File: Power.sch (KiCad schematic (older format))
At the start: 68 parts, among them J3 ESTOP, J4 PWR, J5 Conn_ARM_JTAG_SWD_10, J7 FAN, Q1 MMBT5401LT1G, Q2 PSMN4R8-100BSEJ, Q3 MMBT3904, Q5 PSMN4R8-100BSEJ, Q7 NTS4001NT1G, U10 LMZ21700SIL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

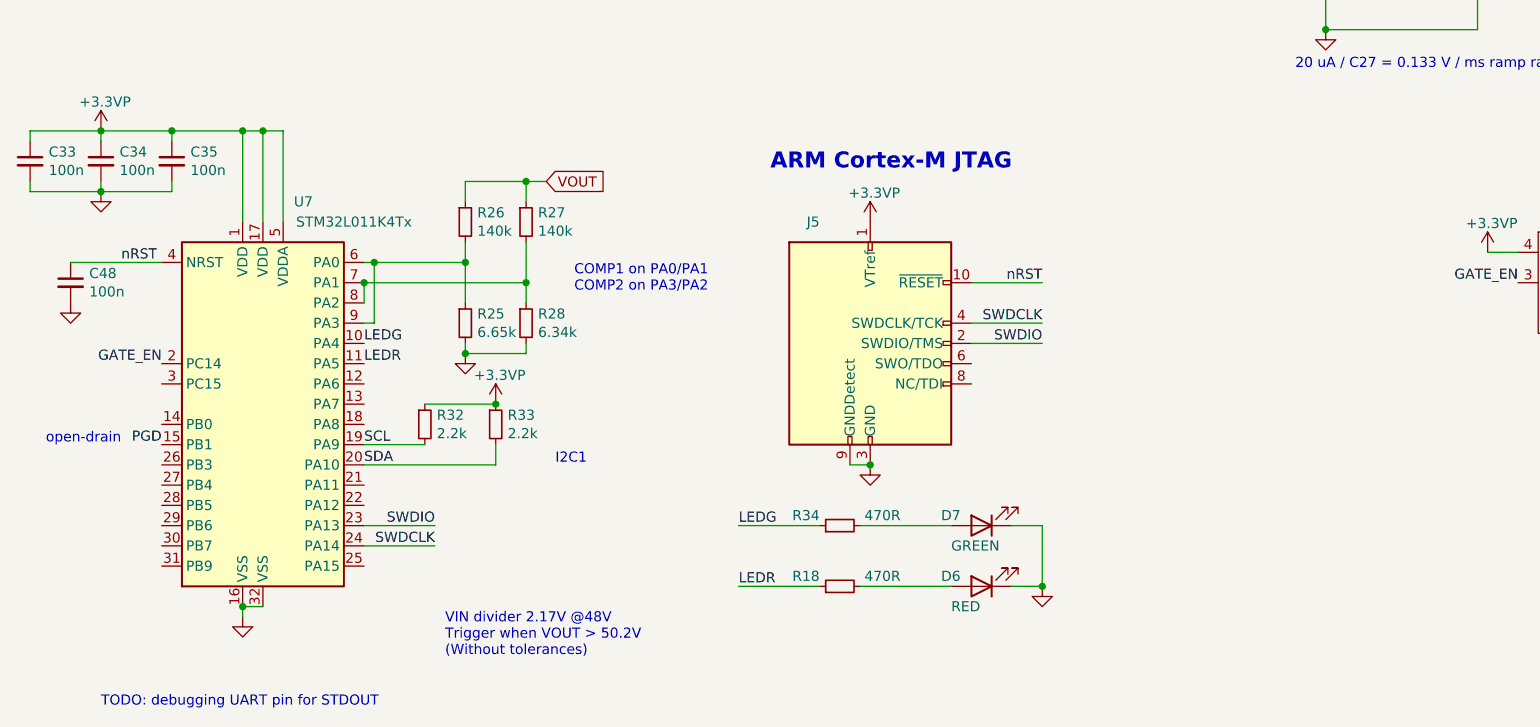
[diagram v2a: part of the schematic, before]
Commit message: layout tweaks. add debugging headers.
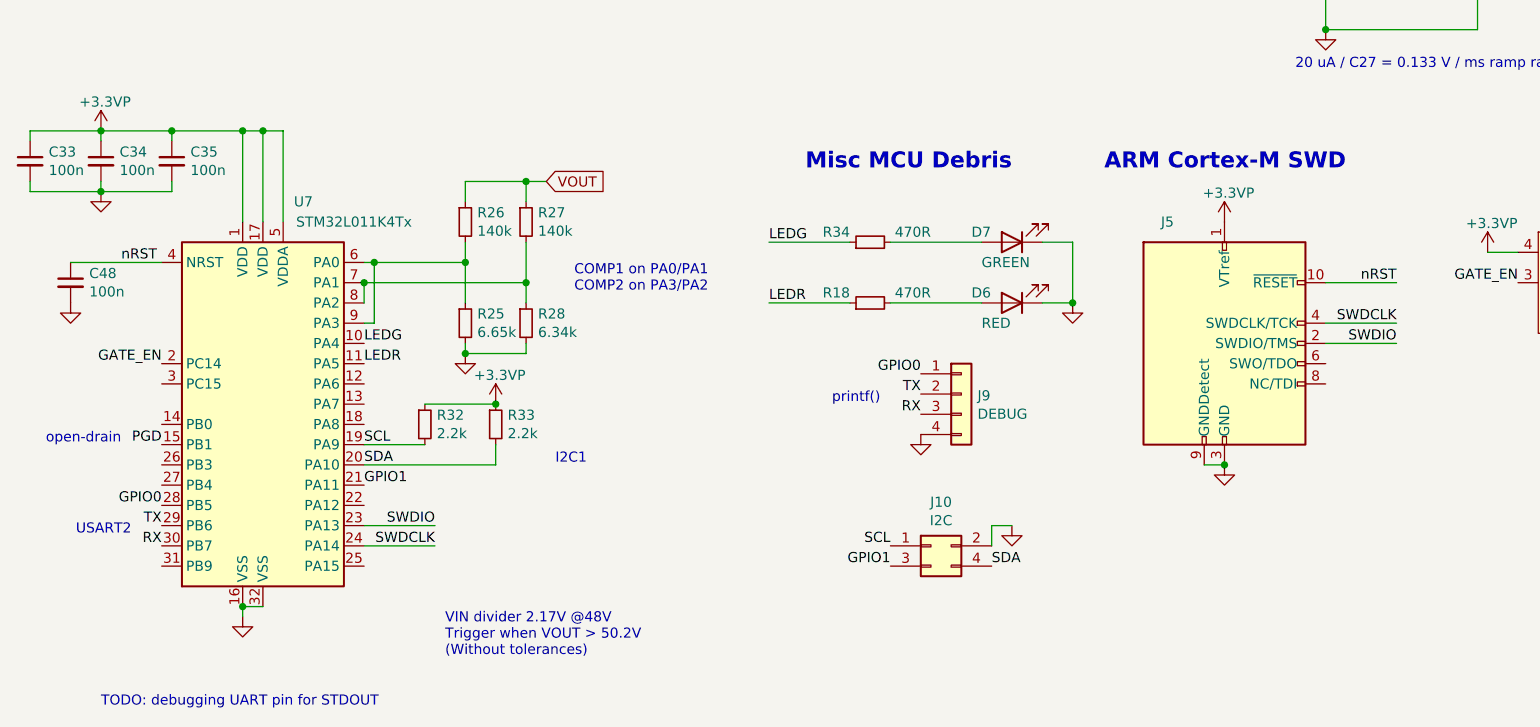
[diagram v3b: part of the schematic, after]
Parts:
- added J10: I2C, Connector_PinHeader_2.54mm:PinHeader_2x02_P2.54mm_Vertical, symbol Connector_Generic:Conn_02x02_Odd_Even
- added J9: DEBUG, Connector_PinHeader_2.54mm:PinHeader_1x04_P2.54mm_Vertical, symbol Connector_Generic:Conn_01x04
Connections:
- net GND: now also J10.2 (Pin_2), J9.4 (Pin_4)
- net SCL: now also J10.1 (Pin_1)
- net SDA: now also J10.4 (Pin_4)
- net GPIO1: now reaches U7.21 (PA11)
- net GPIO1: now also J10.3 (Pin_3)
- net GPIO0: now reaches U7.28 (PB5)
- net GPIO0: now also J9.1 (Pin_1)
- net TX: now reaches U7.29 (PB6)
- net TX: now also J9.2 (Pin_2)
- net RX: now reaches U7.30 (PB7)
- net RX: now also J9.3 (Pin_3)
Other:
- note added: "ARM Cortex-M SWD"
- note added: "Misc MCU Debris"
- note added: "USART2"
- note added: "printf()"
- note removed: "ARM Cortex-M JTAG"
- moved on the sheet: D6, D7, J5, R18, R34
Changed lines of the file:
@@
 Connection ~ 4250 1100
 Connection ~ 4700 1100
-Connection ~ 4800 6400
 Connection ~ 4850 3600
 Connection ~ 5150 1100
@@
 Connection ~ 5450 1450
 Connection ~ 5550 2900
-Connection ~ 5650 7000
+Connection ~ 5800 5600
 Connection ~ 6100 1100
 Connection ~ 6100 1450
 Connection ~ 6550 1100
+Connection ~ 6550 6400
 Connection ~ 6650 3300
 Connection ~ 6925 1100
@@
 	4150 3650 4150 3600
 Wire Wire Line
-	4150 6700 4550 6700
-Wire Wire Line
-	4150 7000 4550 7000
-Wire Wire Line
 	4250 1100 4250 1900
 Wire Wire Line
 	4250 1100 4700 1100
 Wire Wire Line
+	4300 5300 4700 5300
+Wire Wire Line
+	4300 5600 4700 5600
+Wire Wire Line
 	4350 1550 4350 1900
 Wire Wire Line
@@
 	4700 1100 5150 1100
 Wire Wire Line
-	4700 6400 4800 6400
-Wire Wire Line
 	4750 2300 5900 2300
 Wire Wire Line
@@
 	5200 3600 5550 3600
 Wire Wire Line
-	5200 6700 4750 6700
-Wire Wire Line
-	5200 7000 4750 7000
-Wire Wire Line
 	5250 3300 5200 3300
 Wire Wire Line
-	5300 5500 5650 5500
+	5350 5300 4900 5300
+Wire Wire Line
+	5350 5600 4900 5600
+Wire Wire Line
+	5400 6700 5400 6800
 Wire Wire Line
 	5450 1100 6100 1100
@@
 	5450 1400 5450 1450
 Wire Wire Line
-	5500 6700 5650 6700
+	5500 6700 5400 6700
 Wire Wire Line
 	5550 2400 5550 2650
@@
 	5550 3500 5550 3600
 Wire Wire Line
-	5650 5700 5300 5700
-Wire Wire Line
-	5650 5800 5300 5800
-Wire Wire Line
-	5650 6700 5650 7000
-Wire Wire Line
-	5650 7000 5500 7000
+	5650 5300 5800 5300
+Wire Wire Line
+	5800 5300 5800 5600
+Wire Wire Line
+	5800 5600 5650 5600
 Wire Wire Line
 	5900 2650 5900 2300
@@
 	6100 1450 6550 1450
 Wire Wire Line
+	6450 6400 6550 6400
+Wire Wire Line
 	6550 1100 6550 1150
 Wire Wire Line
@@
 	7050 4250 7800 4250
 Wire Wire Line
+	7050 5500 7400 5500
+Wire Wire Line
 	7300 1400 7300 1100
 Wire Wire Line
@@
 Wire Wire Line
 	7300 2700 7500 2700
+Wire Wire Line
+	7400 5700 7050 5700
+Wire Wire Line
+	7400 5800 7050 5800
 Wire Wire Line
 	7500 1100 7500 1400
@@
 Text Notes 1100 6300 2    50   ~ 0
 open-drain
+Text Notes 1150 6750 2    50   ~ 0
+USART2
 Text Notes 1650 3000 0    50   ~ 0
 TODO: gate TVS?
@@
 Text Notes 4000 5550 2    50   ~ 0
 COMP1 on PA0/PA1\nCOMP2 on PA3/PA2
+Text Notes 4850 6100 2    50   ~ 0
+printf()
 Text Notes 4970 3840 0    50   ~ 0
 18.9 V threshold Power Good
@@
 Schottky diode to eat\nkickback energy at power-off
 Text Notes 5500 4950 2    79   ~ 16
-ARM Cortex-M JTAG
+Misc MCU Debris
 Text Notes 5650 3100 2    50   ~ 0
 I2C addr: ZZZ = 0x40
@@
 Text Notes 6850 2200 2    50   ~ 0
 RT floating = 500 kHz
+Text Notes 7150 4950 2    79   ~ 16
+ARM Cortex-M SWD
 Text Notes 8200 4450 2    50   ~ 0
 20 uA / C27 = 0.133 V / ms ramp rate
@@
 Text Label 1300 6300 2    50   ~ 0
 PGD
+Text Label 1300 6600 2    50   ~ 0
+GPIO0
+Text Label 1300 6700 2    50   ~ 0
+TX
+Text Label 1300 6800 2    50   ~ 0
+RX
 Text Label 1700 1100 2    50   ~ 0
 VIN
@@
 Text Label 2300 6400 0    50   ~ 0
 SDA
+Text Label 2300 6500 0    50   ~ 0
+GPIO1
 Text Label 2650 6700 2    50   ~ 0
 SWDIO
@@
 Text Label 3800 1400 0    50   ~ 0
 GATE
-Text Label 4150 6700 0    50   ~ 0
+Text Label 4300 5300 0    50   ~ 0
 LEDG
-Text Label 4150 7000 0    50   ~ 0
+Text Label 4300 5600 0    50   ~ 0
 LEDR
 Text Label 4400 1550 0    50   ~ 0
@@
 Text Label 4800 2100 0    50   ~ 0
 PGD
+Text Label 4900 6800 2    50   ~ 0
+SCL
+Text Label 4900 6900 2    50   ~ 0
+GPIO1
 Text Label 5050 2500 2    50   ~ 0
 LM_VDD
-Text Label 5650 5500 2    50   ~ 0
-nRST
-Text Label 5650 5700 2    50   ~ 0
-SWDCLK
-Text Label 5650 5800 2    50   ~ 0
-SWDIO
+Text Label 5050 5950 2    50   ~ 0
+GPIO0
+Text Label 5050 6050 2    50   ~ 0
+TX
+Text Label 5050 6150 2    50   ~ 0
+RX
+Text Label 5400 6900 0    50   ~ 0
+SDA
 Text Label 6450 3300 0    50   ~ 0
 GATE
+Text Label 7400 5500 2    50   ~ 0
+nRST
+Text Label 7400 5700 2    50   ~ 0
+SWDCLK
+Text Label 7400 5800 2    50   ~ 0
+SWDIO
 Text Label 8000 5500 2    50   ~ 0
 GATE_EN
@@
 L power:+3.3VP #PWR0153
 U 1 1 5D5EB6F2
-P 4800 5200
-F 0 "#PWR0153" H 4950 5150 50  0001 C CNN
-F 1 "+3.3VP" H 4820 5343 50  0000 C CNN
-F 2 "" H 4800 5200 50  0001 C CNN
-F 3 "" H 4800 5200 50  0001 C CNN
-	1    4800 5200
+P 6550 5200
+F 0 "#PWR0153" H 6700 5150 50  0001 C CNN
+F 1 "+3.3VP" H 6570 5343 50  0000 C CNN
+F 2 "" H 6550 5200 50  0001 C CNN
+F 3 "" H 6550 5200 50  0001 C CNN
+	1    6550 5200
 	1    0    0    -1
 $EndComp
@@
 $EndComp
 $Comp
-L power:GND #PWR0139
-U 1 1 5E51739C
-P 4800 6400
-F 0 "#PWR0139" H 4800 6150 50  0001 C CNN
-F 1 "GND" H 4805 6227 50  0001 C CNN
-F 2 "" H 4800 6400 50  0001 C CNN
-F 3 "" H 4800 6400 50  0001 C CNN
-	1    4800 6400
+L power:GND #PWR0152
+U 1 1 5E55447C
+P 5050 6250
+F 0 "#PWR0152" H 5050 6000 50  0001 C CNN
+F 1 "GND" H 5055 6077 50  0001 C CNN
+F 2 "" H 5050 6250 50  0001 C CNN
+F 3 "" H 5050 6250 50  0001 C CNN
+	1    5050 6250
 	-1   0    0    -1
 $EndComp
@@
 $EndComp
 $Comp
+L power:GND #PWR0155
+U 1 1 5E562944
+P 5500 6700
+F 0 "#PWR0155" H 5500 6450 50  0001 C CNN
+F 1 "GND" H 5505 6527 50  0001 C CNN
+F 2 "" H 5500 6700 50  0001 C CNN
+F 3 "" H 5500 6700 50  0001 C CNN
+	1    5500 6700
+	-1   0    0    -1
+$EndComp
+$Comp
 L power:GND #PWR0149
 U 1 1 5E590701
-P 5650 7000
-F 0 "#PWR0149" H 5650 6750 50  0001 C CNN
-F 1 "GND" H 5655 6827 50  0001 C CNN
-F 2 "" H 5650 7000 50  0001 C CNN
-F 3 "" H 5650 7000 50  0001 C CNN
-	1    5650 7000
+P 5800 5600
+F 0 "#PWR0149" H 5800 5350 50  0001 C CNN
+F 1 "GND" H 5805 5427 50  0001 C CNN
+F 2 "" H 5800 5600 50  0001 C CNN
+F 3 "" H 5800 5600 50  0001 C CNN
+	1    5800 5600
+	-1   0    0    -1
+$EndComp
+$Comp
+L power:GND #PWR0139
+U 1 1 5E51739C
+P 6550 6400
+F 0 "#PWR0139" H 6550 6150 50  0001 C CNN
+F 1 "GND" H 6555 6227 50  0001 C CNN
+F 2 "" H 6550 6400 50  0001 C CNN
+F 3 "" H 6550 6400 50  0001 C CNN
+	1    6550 6400
 	-1   0    0    -1
 $EndComp
@@
 L Device:R_Small R34
 U 1 1 5DD84AA4
-P 4650 6700
-F 0 "R34" V 4700 6800 50  0000 L CNN
-F 1 "470R" V 4700 6400 50  0000 L CNN
-F 2 "Resistor_SMD:R_0603_1608Metric" H 4650 6700 50  0001 C CNN
-F 3 "~" H 4650 6700 50  0001 C CNN
-	1    4650 6700
+P 4800 5300
+F 0 "R34" V 4850 5400 50  0000 L CNN
+F 1 "470R" V 4850 5000 50  0000 L CNN
+F 2 "Resistor_SMD:R_0603_1608Metric" H 4800 5300 50  0001 C CNN
+F 3 "~" H 4800 5300 50  0001 C CNN
+	1    4800 5300
 	0    -1   -1   0
 $EndComp
@@
 L Device:R_Small R18
 U 1 1 5E58F9CA
-P 4650 7000
-F 0 "R18" V 4700 7100 50  0000 L CNN
-F 1 "470R" V 4700 6700 50  0000 L CNN
-F 2 "Resistor_SMD:R_0603_1608Metric" H 4650 7000 50  0001 C CNN
-F 3 "~" H 4650 7000 50  0001 C CNN
-	1    4650 7000
+P 4800 5600
+F 0 "R18" V 4850 5700 50  0000 L CNN
+F 1 "470R" V 4850 5300 50  0000 L CNN
+F 2 "Resistor_SMD:R_0603_1608Metric" H 4800 5600 50  0001 C CNN
+F 3 "~" H 4800 5600 50  0001 C CNN
+	1    4800 5600
 	0    -1   -1   0
 $EndComp
@@
 L Device:LED D7
 U 1 1 5DD84AB5
-P 5350 6700
-F 0 "D7" H 5550 6650 50  0000 R CNN
-F 1 "GREEN" H 5500 6800 50  0000 R CNN
-F 2 "LED_SMD:LED_0603_1608Metric" H 5350 6700 50  0001 C CNN
-F 3 "~" H 5350 6700 50  0001 C CNN
-	1    5350 6700
+P 5500 5300
+F 0 "D7" H 5700 5250 50  0000 R CNN
+F 1 "GREEN" H 5650 5400 50  0000 R CNN
+F 2 "LED_SMD:LED_0603_1608Metric" H 5500 5300 50  0001 C CNN
+F 3 "~" H 5500 5300 50  0001 C CNN
+	1    5500 5300
 	-1   0    0    1
 $EndComp
@@
 L Device:LED D6
 U 1 1 5E58F9DF
-P 5350 7000
-F 0 "D6" H 5550 6950 50  0000 R CNN
-F 1 "RED" H 5500 7100 50  0000 R CNN
-F 2 "LED_SMD:LED_0603_1608Metric" H 5350 7000 50  0001 C CNN
-F 3 "~" H 5350 7000 50  0001 C CNN
-	1    5350 7000
+P 5500 5600
+F 0 "D6" H 5700 5550 50  0000 R CNN
+F 1 "RED" H 5650 5700 50  0000 R CNN
+F 2 "LED_SMD:LED_0603_1608Metric" H 5500 5600 50  0001 C CNN
+F 3 "~" H 5500 5600 50  0001 C CNN
+	1    5500 5600
 	-1   0    0    1
 $EndComp
@@
 	1    1350 1200
 	-1   0    0    -1
+$EndComp
+$Comp
+L Connector_Generic:Conn_01x04 J9
+U 1 1 5E553C28
+P 5250 6050
+F 0 "J9" H 5330 6042 50  0000 L CNN
+F 1 "DEBUG" H 5330 5951 50  0000 L CNN
+F 2 "Connector_PinHeader_2.54mm:PinHeader_1x04_P2.54mm_Vertical" H 5250 6050 50  0001 C CNN
+F 3 "~" H 5250 6050 50  0001 C CNN
+	1    5250 6050
+	1    0    0    -1
+$EndComp
+$Comp
+L Connector_Generic:Conn_02x02_Odd_Even J10
+U 1 1 5E569A0C
+P 5100 6800
+F 0 "J10" H 5150 7016 50  0000 C CNN
+F 1 "I2C" H 5150 6925 50  0000 C CNN
+F 2 "Connector_PinHeader_2.54mm:PinHeader_2x02_P2.54mm_Vertical" H 5100 6800 50  0001 C CNN
+F 3 "~" H 5100 6800 50  0001 C CNN
+	1    5100 6800
+	1    0    0    -1
 $EndComp
 $Comp
@@
 L Connector:Conn_ARM_JTAG_SWD_10 J5
 U 1 1 5D5E762E
-P 4800 5800
-F 0 "J5" H 4550 6400 50  0000 R CNN
-F 1 "Conn_ARM_JTAG_SWD_10" H 4357 5755 50  0001 R CNN
-F 2 "Connector_PinHeader_1.27mm:PinHeader_2x05_P1.27mm_Vertical" H 4800 5800 50  0001 C CNN
-F 3 "http://infocenter.arm.com/help/topic/com.arm.doc.ddi0314h/DDI0314H_coresight_components_trm.pdf" V 4450 4550 50  0001 C CNN
-	1    4800 5800
-	1    0    0    -1
-$EndComp
+P 6550 5800
+F 0 "J5" H 6300 6400 50  0000 R CNN
+F 1 "Conn_ARM_JTAG_SWD_10" H 6107 5755 50  0001 R CNN
+F 2 "Connector_PinHeader_1.27mm:PinHeader_2x05_P1.27mm_Vertical" H 6550 5800 50  0001 C CNN
+F 3 "http://infocenter.arm.com/help/topic/com.arm.doc.ddi0314h/DDI0314H_coresight_components_trm.pdf" V 6200 4550 50  0001 C CNN
+	1    6550 5800
+	1    0    0    -1
+$EndComp

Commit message: ready to generate CAM
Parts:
- C27: D1N (none) -> Digikey; D1PN (none) -> 399-17949-1-ND; MFN (none) -> KEMET; MPN (none) -> C1206C154KARACAUTO; Maximum Voltage (none) -> 250 V; Tolerance (none) -> 10%
- C28: D1N (none) -> Digikey; D1PN (none) -> 478-1529-1-ND; MFN (none) -> AVX; MPN (none) -> 12061C104KAT2A; Maximum Voltage (none) -> 100 V; Tolerance (none) -> 10%
- C29, C30: value 1uF -> 1u; D1N (none) -> Digikey; D1PN (none) -> 311-1445-1-ND; MFN (none) -> Yageo; MPN (none) -> CC0603KRX5R8BB105
- C31, C33, C34, C35, C47, C48: D1N (none) -> Digikey; D1PN (none) -> 311-1344-1-ND; MFN (none) -> Yageo; MPN (none) -> CC0603KRX7R9BB104
- C32: Maximum Voltage (none) -> 80 V; Tolerance (none) -> 20%
- C36: value 1nF -> 1n; D1N (none) -> Digikey; D1PN (none) -> 311-1080-1-ND; MFN (none) -> Yageo; MPN (none) -> CC0603KRX7R9BB102
- C37, C39: D1N (none) -> Digikey; D1PN (none) -> 311-1445-1-ND; MFN (none) -> Yageo; MPN (none) -> CC0603KRX5R8BB105
- C38: D1N (none) -> Digikey; D1PN (none) -> 311-1451-1-ND; MFN (none) -> Yageo; MPN (none) -> CC0603KRX5R6BB225; Maximum Voltage (none) -> 10 V; Tolerance (none) -> 10%
- C40: footprint Capacitor_SMD:C_1210_3225Metric -> Capacitor_SMD:C_1206_3216Metric; D1N (none) -> Digikey; D1PN (none) -> 490-18620-1-ND; MFN (none) -> Murata; MPN (none) -> GRM31CC72A475KE11L; Maximum Voltage (none) -> 100 V; Tolerance (none) -> 10%
- C41: D1N (none) -> Digikey; D1PN (none) -> 311-3365-1-ND; MFN (none) -> Yageo; MPN (none) -> CC0603KRX5R8BB474; Maximum Voltage (none) -> 25 V; Tolerance (none) -> 10%
- C42: footprint Capacitor_SMD:C_1210_3225Metric -> Capacitor_SMD:C_1206_3216Metric; Capacitance 22u -> (none); D1PN 1276-1101-1-ND -> 1276-3047-1-ND; MPN CL32A226KAJNNNE -> CL31A226KAHNNNE; Maximum Voltage 25V -> 25 V
- C43: Capacitance 22u -> (none); D1PN 1276-1101-1-ND -> 1276-3047-1-ND; MPN CL32A226KAJNNNE -> CL31A226KAHNNNE; Maximum Voltage 25V -> 25 V
- C44: Capacitance 4n7 -> (none); D1PN (none) -> 311-3366-1-ND; MFN (none) -> Yageo; MPN (none) -> CC0603KRX7R0BB472; Maximum Voltage 25V -> 25 V
- C45: Capacitance 22u -> (none); D1PN 1276-1101-1-ND -> 490-5528-1-ND; MFN Samsung -> Murata; MPN CL32A226KAJNNNE -> GRM31CR61A476ME15L; Maximum Voltage 6.3V -> 10 V
- C46: D1N (none) -> Digikey; D1PN (none) -> 1276-2344-1-ND; MFN (none) -> Samsung; MPN (none) -> CL10C820JC81PNC; Maximum Voltage (none) -> 100 V; Tolerance (none) -> 5%
- D6: D1N (none) -> Digikey; D1PN (none) -> 732-4978-1-ND; MFN (none) -> Wurth; MPN (none) -> 150060RS75000
- D7: D1N (none) -> Digikey; D1PN (none) -> 732-4980-1-ND; MFN (none) -> Wurth; MPN (none) -> 150060VS75000
- J10, J9: D1N (none) -> DNP; D1PN (none) -> DNP; MFN (none) -> DNP; MPN (none) -> DNP
- J3: D1N (none) -> Digikey; D1PN (none) -> WM15141-ND; MFN (none) -> Molex; MPN (none) -> 1053131302
- J4: D1N (none) -> Digikey; D1PN (none) -> WM14310CT-ND; MFN (none) -> Molex; MPN (none) -> 436500214
- J5: D1N (none) -> Digikey; D1PN (none) -> S9015E-05-ND; MFN (none) -> Sullins; MPN (none) -> GRPB052VWVN-RC
- J7: D1N digikey -> Digikey; MPN 0022232031 -> 22232031
- L1: D1N (none) -> Digikey; D1PN (none) -> 732-1199; MFN (none) -> Wurth; MPN (none) -> 744777920
- Q5: D1N (none) -> Digikey; D1PN (none) -> 1727-1103-1-ND; MFN (none) -> NXP; MPN (none) -> PSMN4R8-100BSEJ
- R10, R12, R15, R26, R27: D1N (none) -> Digikey; D1PN (none) -> P140KDBCT-ND; MFN (none) -> Panasonic; MPN (none) -> ERA-3AEB1403V; Tolerance (none) -> 0.1%
- R11: value 6k5 -> 6k49; D1N (none) -> Digikey; D1PN (none) -> P6.49KDBCT-ND; MFN (none) -> Panasonic; MPN (none) -> ERA-3AEB6491V; Tolerance (none) -> 0.1%
- R13: D1N (none) -> Digikey; D1PN (none) -> P25.5KDBCT-ND; MFN (none) -> Panasonic; MPN (none) -> ERA-3AEB2552V; Tolerance (none) -> 0.1%
- R16, R17: D1N (none) -> Digikey; D1PN (none) -> P21KDBCT-ND; MFN (none) -> Panasonic; MPN (none) -> ERA-3AEB2102V; Tolerance (none) -> 0.1%
- R18, R34: D1N (none) -> Digikey; D1PN (none) -> 311-470HRCT-ND; MFN (none) -> Yageo; MPN (none) -> RC0603FR-07470RL; Tolerance (none) -> 1%
- R19: D1N (none) -> Digikey; D1PN (none) -> 311-33.0HRCT-ND; MFN (none) -> Yageo; MPN (none) -> RC0603FR-0733RL; Tolerance (none) -> 1%
- R21: D1N (none) -> Digikey; D1PN (none) -> 696-1107-5-ND; MFN (none) -> Riedon; MPN (none) -> PF2472-10RF1
- R24: D1PN 311-453KHRCT-ND -> 311-1.00MHRCT-ND; MPN RC0603FR-07453KL -> RC0603FR-071ML; Maximum Power 0.1W -> (none); Resistance 1100000.0ohm -> (none)
- R25: D1N (none) -> Digikey; D1PN (none) -> P6.65KDBCT-ND; MFN (none) -> Panasonic; MPN (none) -> ERA-3AEB6651V; Tolerance (none) -> 0.1%
- R28: D1N (none) -> Digikey; D1PN (none) -> P6.34KDBCT-ND; MFN (none) -> Panasonic; MPN (none) -> ERA-3AEB6341V; Tolerance (none) -> 0.1%
- R29: D1PN P49.9KHCT-ND -> 311-1.91KHRCT-ND; MFN Panasonic -> Yageo; MPN ERJ-3EKF4992V -> RC0603FR-071K91L; Maximum Power 0.1W -> (none); Resistance 124000.0ohm -> (none)
- R30: D1PN (none) -> 311-432KHRCT-ND; MFN (none) -> Yageo; MPN (none) -> RC0603FR-07432KL; Resistance 432000 -> (none)
- R31: D1PN (none) -> P140KDBCT-ND; MFN (none) -> Panasonic; MPN (none) -> ERA-3AEB1403V; Tolerance 1% -> 0.1%
- R32, R33: D1N (none) -> Digikey; D1PN (none) -> 311-2.20KHRCT-ND; MFN (none) -> Yageo; MPN (none) -> RC0603FR-072K2L; Tolerance (none) -> 1%
- R35, R9: D1N (none) -> Digikey; D1PN (none) -> 311-1.00KHRCT-ND; MFN (none) -> Yageo; MPN (none) -> RC0603FR-071KL; Tolerance (none) -> 1%
- R36: D1N (none) -> Digikey; D1PN (none) -> 311-10KGRCT-ND; MFN (none) -> Yageo; MPN (none) -> RC0603JR-0710KL
- R37: D1N (none) -> Digikey; D1PN (none) -> 311-100KHRCT-ND; MFN (none) -> Yageo; MPN (none) -> RC0603FR-07100KL; Tolerance (none) -> 1%
- U7: value STM32L011K4Tx -> STM32L071KZT6; D1N (none) -> Digikey; D1PN (none) -> 497-18578-ND; MFN (none) -> ST; MPN (none) -> STM32L071KZT6
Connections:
- net GND: now also U7.31 (PB9)
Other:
- note added: "PB9 = BOOT0\nlow = run from flash"
- note removed: "TODO: debugging UART pin for STDOUT"
